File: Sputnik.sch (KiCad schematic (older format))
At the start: 0 parts

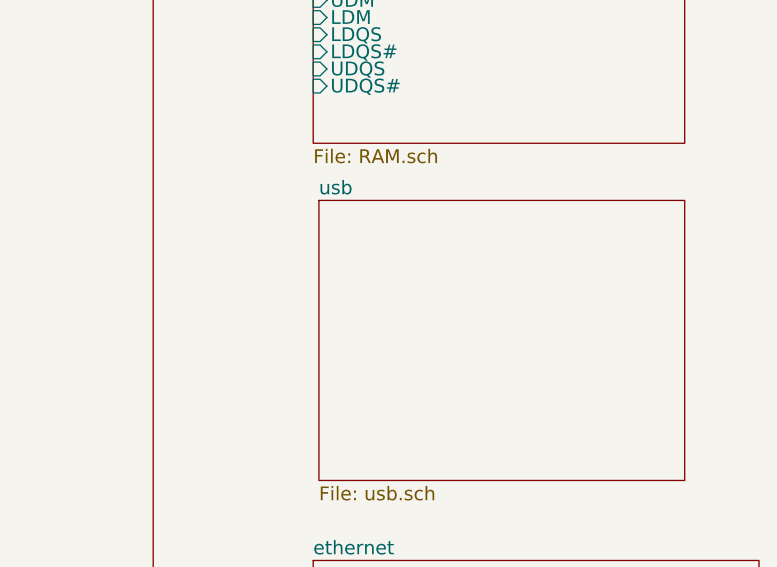
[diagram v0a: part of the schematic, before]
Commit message: More USB signals
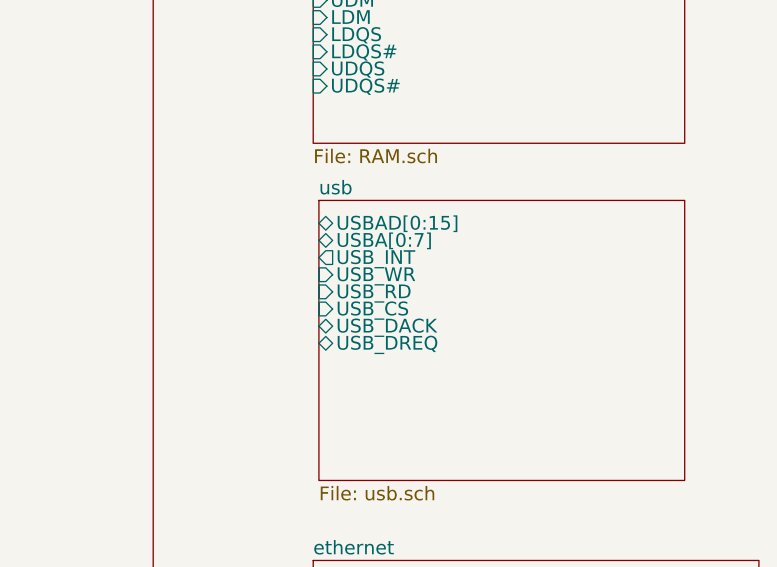
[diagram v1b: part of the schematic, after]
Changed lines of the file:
@@
 F0 "usb" 60
 F1 "usb.sch" 60
+F2 "USBAD[0:15]" B L 11325 2775 60
+F3 "USBA[0:7]" B L 11325 2850 60
+F4 "USB_INT" O L 11325 2925 60
+F5 "USB_WR" I L 11325 3000 60
+F6 "USB_RD" I L 11325 3075 60
+F7 "USB_CS" I L 11325 3150 60
+F8 "USB_DACK" B L 11325 3225 60
+F9 "USB_DREQ" B L 11325 3300 60
 $EndSheet
 $EndSCHEMATC

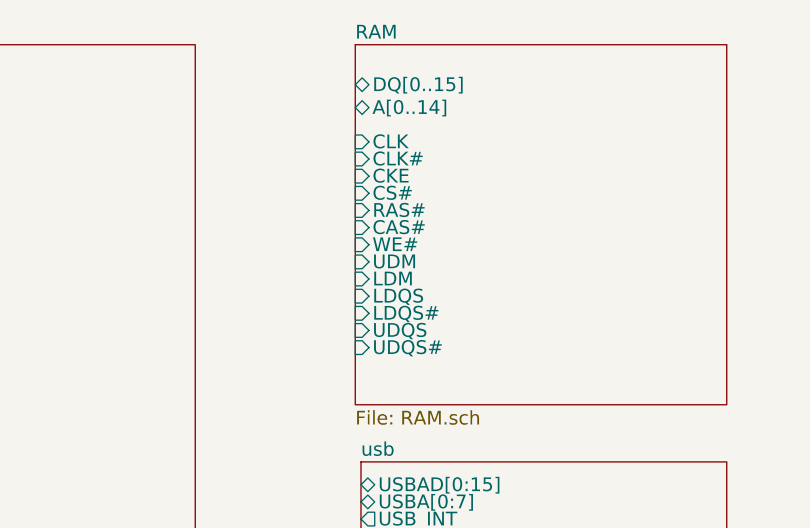
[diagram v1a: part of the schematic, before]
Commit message: Start fitting DDR2
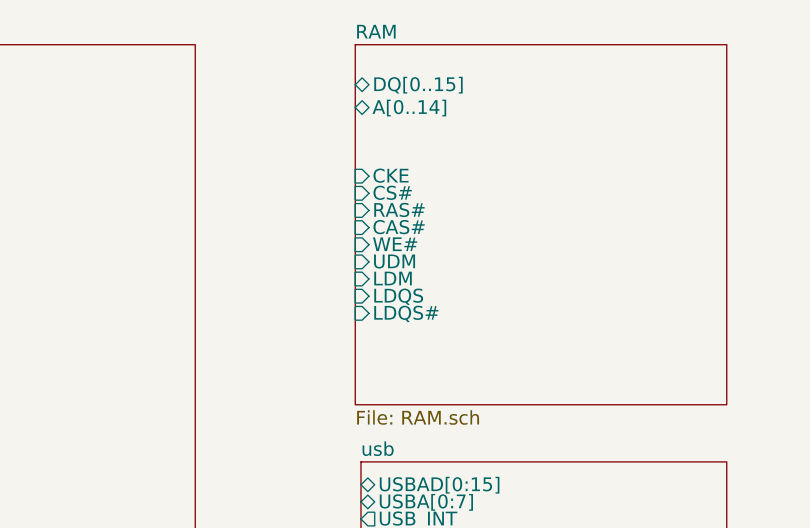
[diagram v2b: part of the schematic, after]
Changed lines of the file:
@@
 LIBS:Stream
 LIBS:ep4ce10f17
+LIBS:Winbond
 LIBS:Sputnik-cache
 EELAYER 25 0
@@
 F2 "DQ[0..15]" B L 11300 1025 60
 F3 "A[0..14]" B L 11300 1125 60
-F4 "CLK" I L 11300 1275 60
-F5 "CLK#" I L 11300 1350 60
-F6 "CKE" I L 11300 1425 60
-F7 "CS#" I L 11300 1500 60
-F8 "RAS#" I L 11300 1575 60
-F9 "CAS#" I L 11300 1650 60
-F10 "WE#" I L 11300 1725 60
-F11 "UDM" I L 11300 1800 60
-F12 "LDM" I L 11300 1875 60
-F13 "LDQS" I L 11300 1950 60
-F14 "LDQS#" I L 11300 2025 60
-F15 "UDQS" I L 11300 2100 60
-F16 "UDQS#" I L 11300 2175 60
-$EndSheet
-Wire Wire Line
+F4 "CKE" I L 11300 1425 60
+F5 "CS#" I L 11300 1500 60
+F6 "RAS#" I L 11300 1575 60
+F7 "CAS#" I L 11300 1650 60
+F8 "WE#" I L 11300 1725 60
+F9 "UDM" I L 11300 1800 60
+F10 "LDM" I L 11300 1875 60
+F11 "LDQS" I L 11300 1950 60
+F12 "LDQS#" I L 11300 2025 60
+$EndSheet
+Wire Wire Line

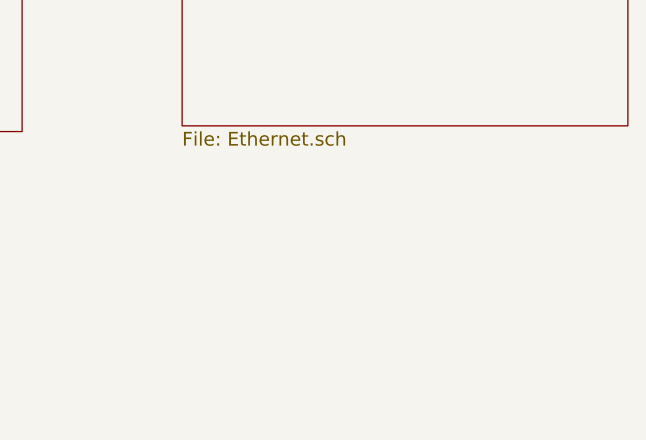
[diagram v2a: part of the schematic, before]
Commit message: Added power sheet, 1V8 chip docs etc
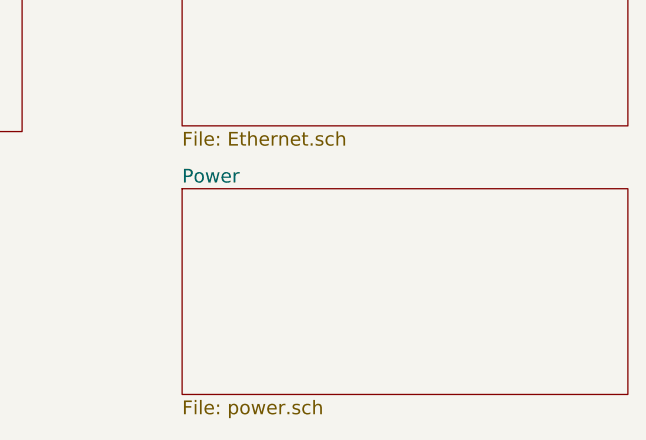
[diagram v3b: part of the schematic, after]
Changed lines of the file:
@@
 $Descr A3 16535 11693
 encoding utf-8
-Sheet 1 6
+Sheet 1 7
 Title ""
 Date ""
@@
 F9 "USB_DREQ" B L 11325 3300 60
 $EndSheet
+$Sheet
+S 11300 6225 1950 900
+U 588C9C43
+F0 "Power" 60
+F1 "power.sch" 60
+$EndSheet
 $EndSCHEMATC

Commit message: A bit of routing
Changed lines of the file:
@@
 F43 "ETHSD[0..15]" B R 10600 4350 60
 $EndSheet
-Wire Bus Line
-	4600 1550 3100 1550
-Wire Bus Line
-	3100 1700 4600 1700
-Wire Bus Line
-	3100 1850 4600 1850
-Wire Bus Line
-	3100 1950 4600 1950
-Wire Wire Line
-	3100 1075 4600 1075
-Wire Wire Line
-	4600 1150 3100 1150
-Wire Wire Line
-	3100 1225 4600 1225
-Wire Wire Line
-	3100 1300 4600 1300
-Wire Wire Line
-	4600 1375 3100 1375
-Wire Wire Line
-	3100 2225 4600 2225
-Wire Wire Line
-	4600 2300 3100 2300
-Wire Wire Line
-	4600 2375 3100 2375
-Wire Wire Line
-	3100 2450 4600 2450
-Wire Bus Line
-	4600 2050 3100 2050
 Text Notes 5200 4525 0    50   ~ 0
 6.1.3 Open Collector Signals\nMany of the bus signals are shared via open collector or open drain outputs rather than via\ntri-stated signals; this is of course required for some asynchronous things like the shared interrupt\nlines, and it works well for other types of signals as well. Of course, a backplane resistor pulls\nthese lines high, PICs only drive the line low.\n\n/OWN /DTACK /HLT /BGACK\n/RESET /CINH /INT 2 /BERR /INT 6
@@
 F37 "nDTACK" O R 3100 3925 60
 $EndSheet
+$Sheet
+S 11300 4250 1950 1700
+U 57F77ED3
+F0 "ethernet" 60
+F1 "Ethernet.sch" 60
+F2 "CMD" I L 11300 4800 60
+F3 "INT" O L 11300 4950 60
+F4 "IOR#" I L 11300 5025 60
+F5 "IOW#" I L 11300 5100 60
+F6 "CS#" I L 11300 5175 60
+F7 "PWRST#" I L 11300 5250 60
+F8 "ETHSD[0..15]" B L 11300 4350 60
+$EndSheet
+$Sheet
+S 11300 850  1625 1575
+U 57FAA395
+F0 "RAM" 60
+F1 "RAM.sch" 60
+F2 "DQ[0..15]" B L 11300 1025 60
+F3 "A[0..14]" B L 11300 1125 60
+F4 "CKE" I L 11300 1425 60
+F5 "CS#" I L 11300 1500 60
+F6 "RAS#" I L 11300 1575 60
+F7 "CAS#" I L 11300 1650 60
+F8 "WE#" I L 11300 1725 60
+F9 "UDM" I L 11300 1800 60
+F10 "LDM" I L 11300 1875 60
+F11 "LDQS" I L 11300 1950 60
+F12 "LDQS#" I L 11300 2025 60
+$EndSheet
+$Sheet
+S 11325 2675 1600 1225
+U 587F5FE1
+F0 "usb" 60
+F1 "usb.sch" 60
+$EndSheet
+$Sheet
+S 11300 6225 1950 900
+U 588C9C43
+F0 "Power" 60
+F1 "power.sch" 60
+$EndSheet
+Wire Bus Line
+	4600 1550 3100 1550
+Wire Bus Line
+	3100 1700 4600 1700
+Wire Bus Line
+	3100 1850 4600 1850
+Wire Bus Line
+	3100 1950 4600 1950
+Wire Wire Line
+	3100 1075 4600 1075
+Wire Wire Line
+	4600 1150 3100 1150
+Wire Wire Line
+	3100 1225 4600 1225
+Wire Wire Line
+	3100 1300 4600 1300
+Wire Wire Line
+	4600 1375 3100 1375
+Wire Wire Line
+	3100 2225 4600 2225
+Wire Wire Line
+	4600 2300 3100 2300
+Wire Wire Line
+	4600 2375 3100 2375
+Wire Wire Line
+	3100 2450 4600 2450
+Wire Bus Line
+	4600 2050 3100 2050
 Wire Wire Line
 	4600 3925 3100 3925
@@
 Wire Wire Line
 	4600 4725 3100 4725
-$Sheet
-S 11300 4250 1950 1700
-U 57F77ED3
-F0 "ethernet" 60
-F1 "Ethernet.sch" 60
-F2 "CMD" I L 11300 4800 60
-F3 "INT" O L 11300 4950 60
-F4 "IOR#" I L 11300 5025 60
-F5 "IOW#" I L 11300 5100 60
-F6 "CS#" I L 11300 5175 60
-F7 "PWRST#" I L 11300 5250 60
-F8 "ETHSD[0..15]" B L 11300 4350 60
-$EndSheet
 Wire Wire Line
 	3100 2525 4600 2525
@@
 Wire Wire Line
 	4600 3700 3100 3700
-$Sheet
-S 11300 850  1625 1575
-U 57FAA395
-F0 "RAM" 60
-F1 "RAM.sch" 60
-F2 "DQ[0..15]" B L 11300 1025 60
-F3 "A[0..14]" B L 11300 1125 60
-F4 "CKE" I L 11300 1425 60
-F5 "CS#" I L 11300 1500 60
-F6 "RAS#" I L 11300 1575 60
-F7 "CAS#" I L 11300 1650 60
-F8 "WE#" I L 11300 1725 60
-F9 "UDM" I L 11300 1800 60
-F10 "LDM" I L 11300 1875 60
-F11 "LDQS" I L 11300 1950 60
-F12 "LDQS#" I L 11300 2025 60
-$EndSheet
 Wire Wire Line
 	3100 3375 4600 3375
@@
 Wire Bus Line
 	10600 4350 11300 4350
-$Sheet
-S 11325 2675 1600 1225
-U 587F5FE1
-F0 "usb" 60
-F1 "usb.sch" 60
-F2 "USBAD[0:15]" B L 11325 2775 60
-F3 "USBA[0:7]" B L 11325 2850 60
-F4 "USB_INT" O L 11325 2925 60
-F5 "USB_WR" I L 11325 3000 60
-F6 "USB_RD" I L 11325 3075 60
-F7 "USB_CS" I L 11325 3150 60
-F8 "USB_DACK" B L 11325 3225 60
-F9 "USB_DREQ" B L 11325 3300 60
-$EndSheet
-$Sheet
-S 11300 6225 1950 900
-U 588C9C43
-F0 "Power" 60
-F1 "power.sch" 60
-$EndSheet
 $EndSCHEMATC
